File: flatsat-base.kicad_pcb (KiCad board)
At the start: 2 copper layers, 228.6 x 134.6 mm, 23 parts, among them J1 FFC2B28-24-G, J10 Conn_01x24_Male, J11 Conn_01x10_Male, J12 FFC2B28-10-G, J2 FFC2B28-10-G, J3 FFC2B28-10-G, J4 FFC2B28-10-G, J5 FFC2B28-10-G, J6 FFC2B28-10-G, J7 FFC2B28-10-G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

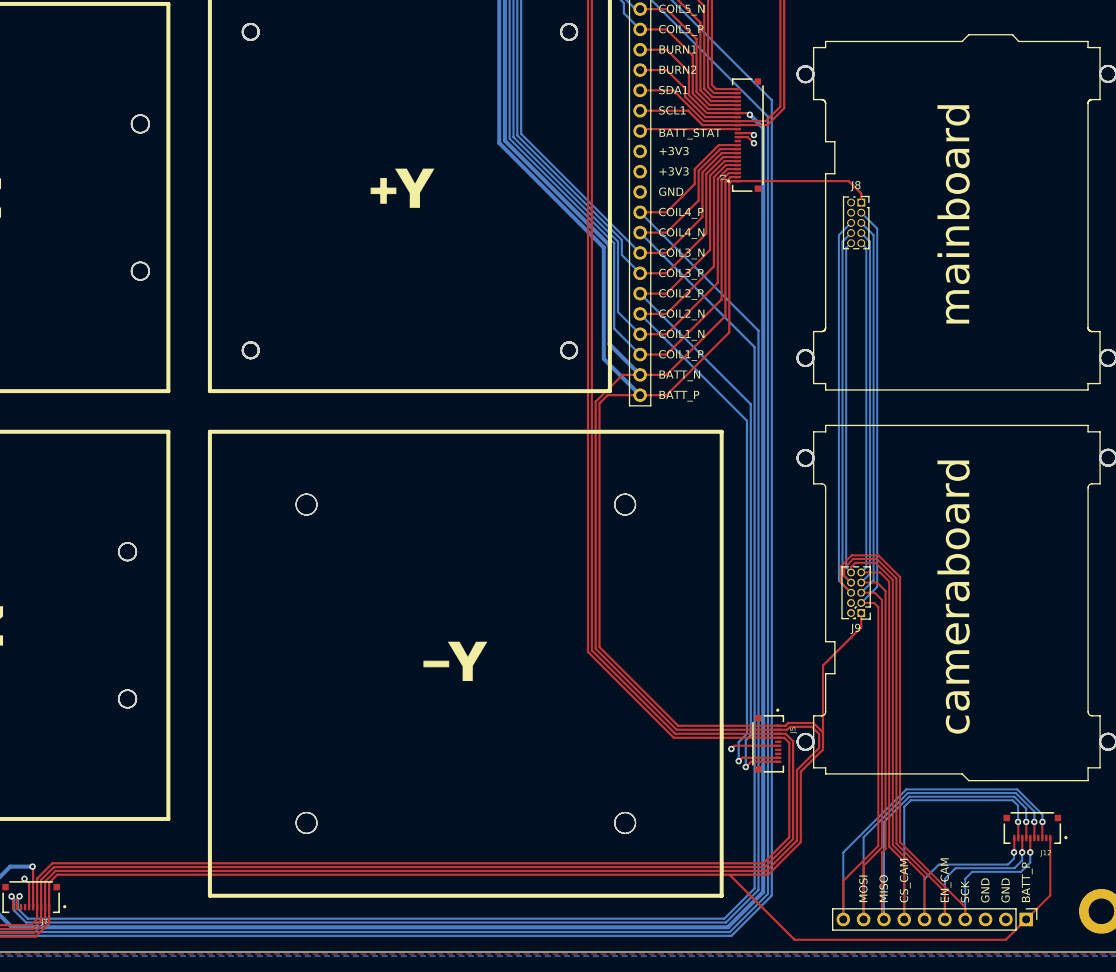
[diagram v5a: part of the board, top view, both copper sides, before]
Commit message: Fixed some clearance issues, and re-routed Batt_P line
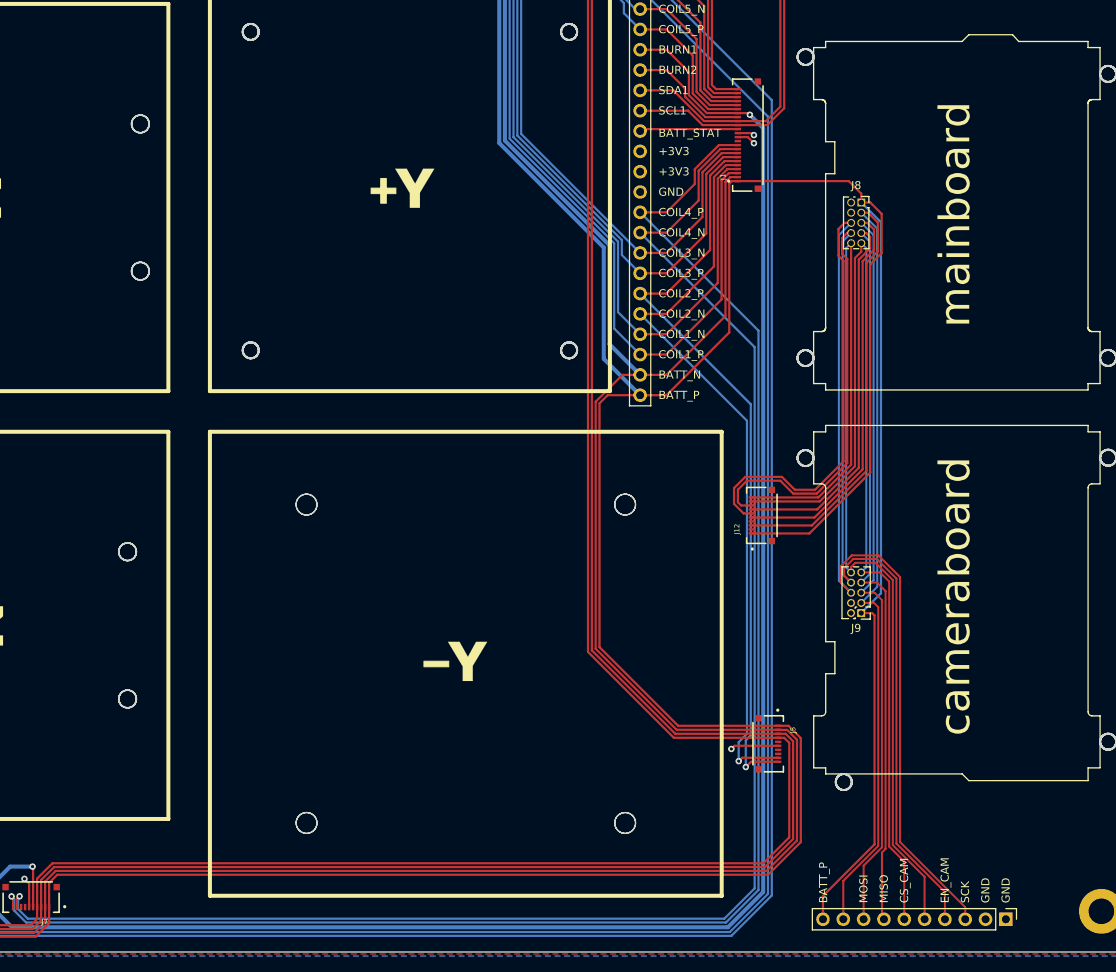
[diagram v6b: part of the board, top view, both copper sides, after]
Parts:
- moved J12 51.7 mm to (203.9, 84.6), turned to 90 degrees
- moved J11 2.54 mm to (234.4, 135.1)
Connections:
- J11 pad 1: BATT_P -> GND
- J11 pad 10: CAM_P3 -> BATT_P
- J11 pad 3: GND -> SCK
- J11 pad 4: SCK -> EN_CAM
- J11 pad 5: EN_CAM -> CAM_P10
- J11 pad 6: CAM_P10 -> CS_CAM
- J11 pad 7: CS_CAM -> MISO
- J11 pad 8: MISO -> MOSI
- J11 pad 9: MOSI -> CAM_P3
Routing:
- net BATT_P: track 569.5 -> 644.5 mm
- net SCK: track 123.7 -> 158.9 mm, vias 1 -> 0
- net EN_CAM: track 118.4 -> 149.5 mm, vias 1 -> 0
- net CAM_P10: track 112.6 -> 134.5 mm, vias 1 -> 0
- net MISO: track 124.8 -> 135.5 mm, vias 1 -> 0
- net MOSI: track 129.5 -> 140.2 mm, vias 1 -> 0
- net CAM_P3: track 134.4 -> 145.0 mm, vias 1 -> 0
- net CS_CAM: track 121.6 -> 131.6 mm, vias 1 -> 0
- net BATT_N: track 477.4 -> 472.8 mm
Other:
- outline, holes or cut-outs redrawn

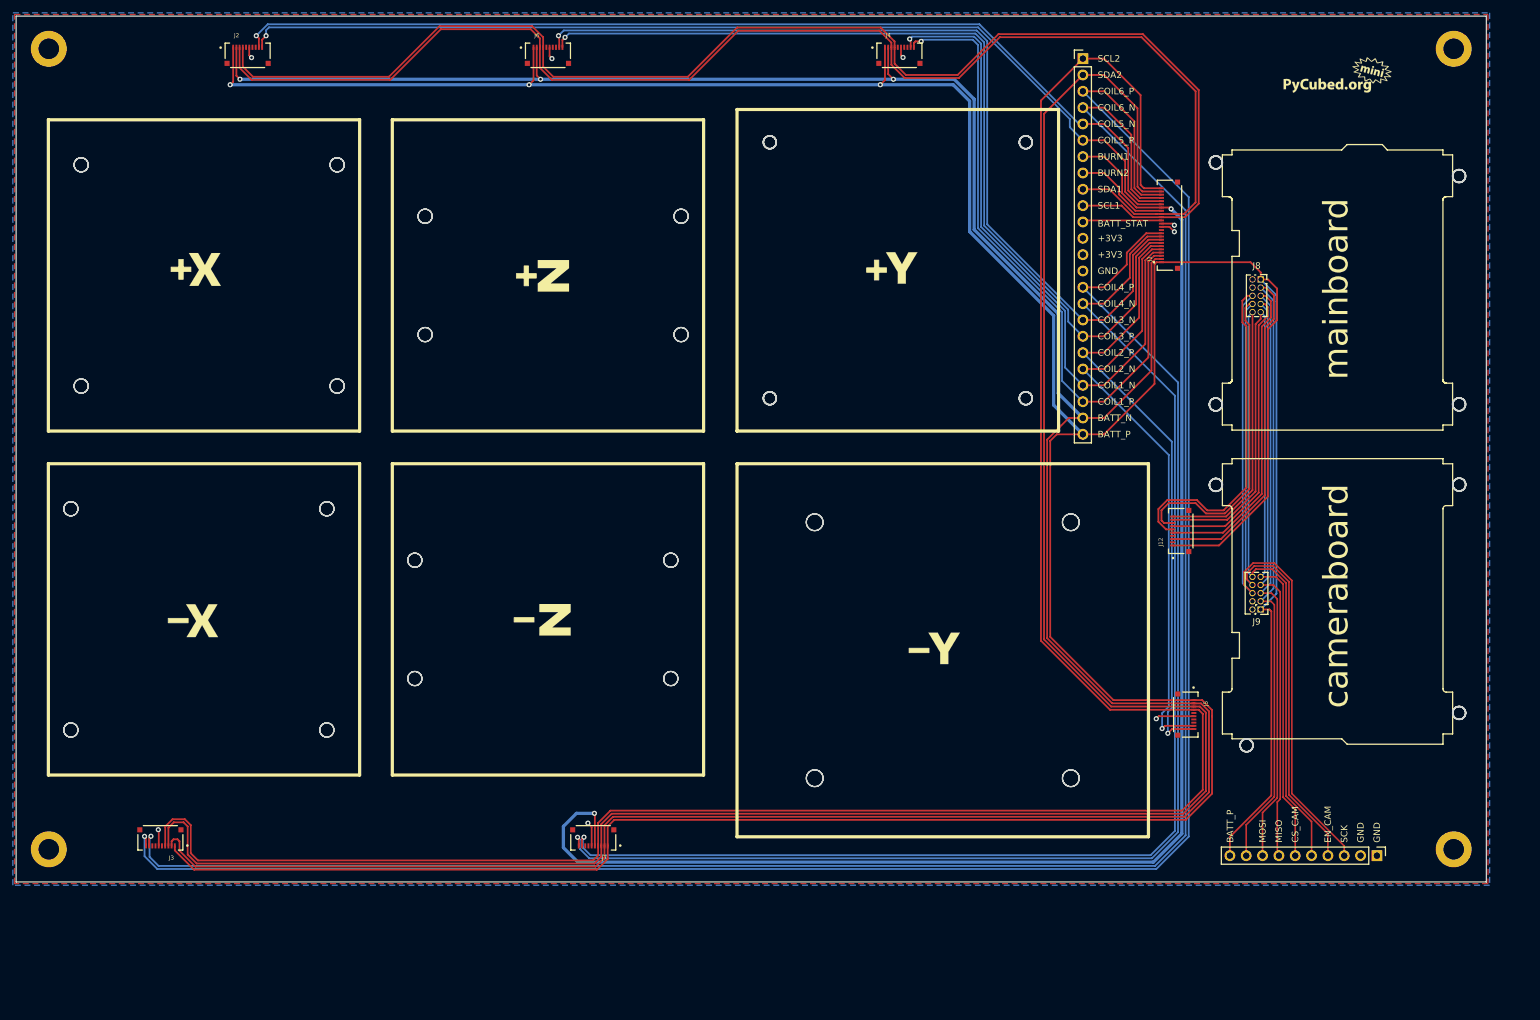
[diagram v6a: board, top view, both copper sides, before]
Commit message: Separated Batt_P and Cam_Batt_P, added FFC connector and realigned
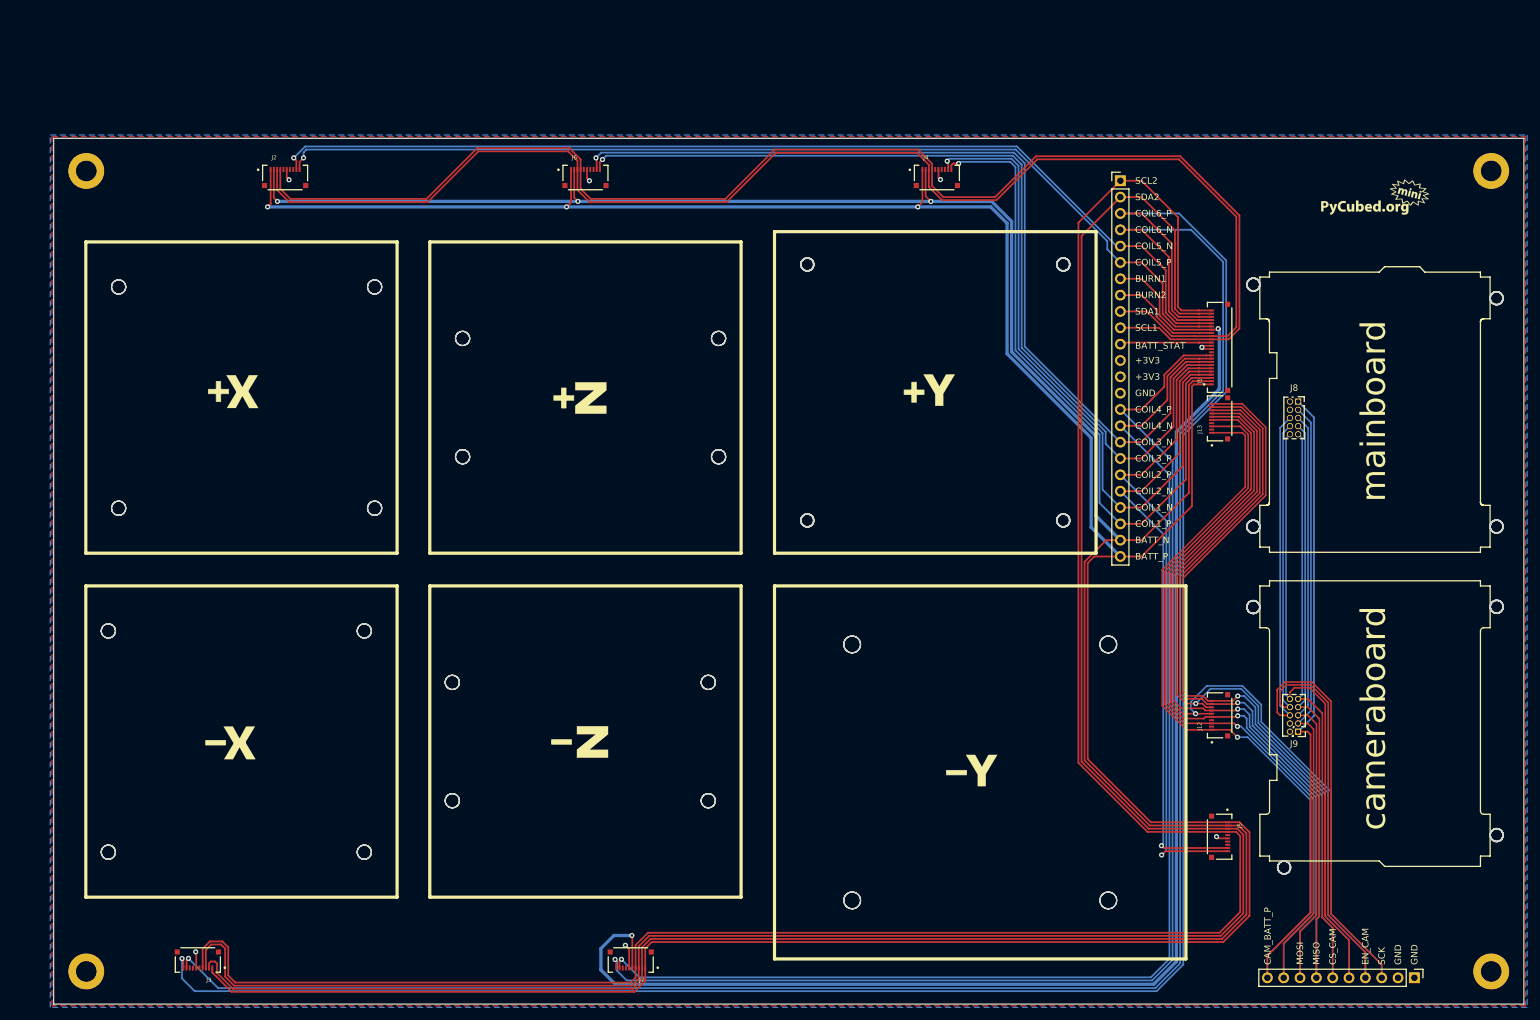
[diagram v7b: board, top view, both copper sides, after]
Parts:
- added J13: FFC2B28-10-G, solarpanels:GCT_FFC2B28-10-G, F.Cu at (210.0, 67.1)
- moved J12 29.3 mm to (210.0, 113.3)
- moved J1 20.5 mm to (210.0, 56.1)
- moved REF** 19.9 mm to (57.6, 119.1)
- moved J8 19.9 mm to (222.2, 64.5)
- moved Ref** 19.9 mm to (190.0, 122.8)
- moved J2 19.9 mm to (64.7, 29.7)
- moved J3 19.9 mm to (51.1, 151.3)
- moved J7 19.9 mm to (118.4, 151.3)
- moved Ref** 19.9 mm to (111.8, 117.2)
- moved H1 19.9 mm to (33.8, 28.6)
- moved H2 19.9 mm to (33.8, 153.1)
- moved H3 19.9 mm to (252.2, 153.1)
- moved H4 19.9 mm to (252.2, 28.6)
- moved J10 19.9 mm to (194.5, 30.2)
- moved J11 19.9 mm to (240.3, 154.1)
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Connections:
- J11 pad 10: BATT_P -> CAM_BATT_P
- J12 pad 1: BATT_P -> CAM_BATT_P
- J8 pad 1: BATT_P -> CAM_BATT_P
- J9 pad 1: BATT_P -> CAM_BATT_P
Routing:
- net CAM_BATT_P: track 0.00 -> 208.4 mm, vias 0 -> 1
- net BATT_P: track 644.5 -> 479.5 mm
- net SCK: track 158.9 -> 237.1 mm, vias 0 -> 1
- net CAM_P10: track 134.5 -> 211.2 mm, vias 0 -> 1
- net EN_CAM: track 149.5 -> 225.0 mm, vias 0 -> 1
- net CS_CAM: track 131.6 -> 203.3 mm, vias 0 -> 1
- net MISO: track 135.5 -> 203.1 mm, vias 0 -> 1
- net MOSI: track 140.2 -> 205.2 mm, vias 0 -> 1
- net CAM_P3: track 145.0 -> 206.2 mm, vias 0 -> 1
- net COIL4_N: track 203.9 -> 195.8 mm
- net COIL4_P: track 206.3 -> 199.3 mm
- net +3V3: track 22.2 -> 16.8 mm, vias 8 -> 7
- net COIL2_P: track 94.0 -> 99.4 mm
- net COIL6_P: track 317.5 -> 321.5 mm
- net COIL2_N: track 93.4 -> 96.9 mm
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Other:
- board text added: "CAM_BATT_P"
